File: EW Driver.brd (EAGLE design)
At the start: 103.9 x 81.8 mm, 42 parts, among them Q1 IRF840S, U1 MAX1771ESA, U2 ARDUINOMICRO, U5 HV507, U6 HV507, X1 BNCHOR

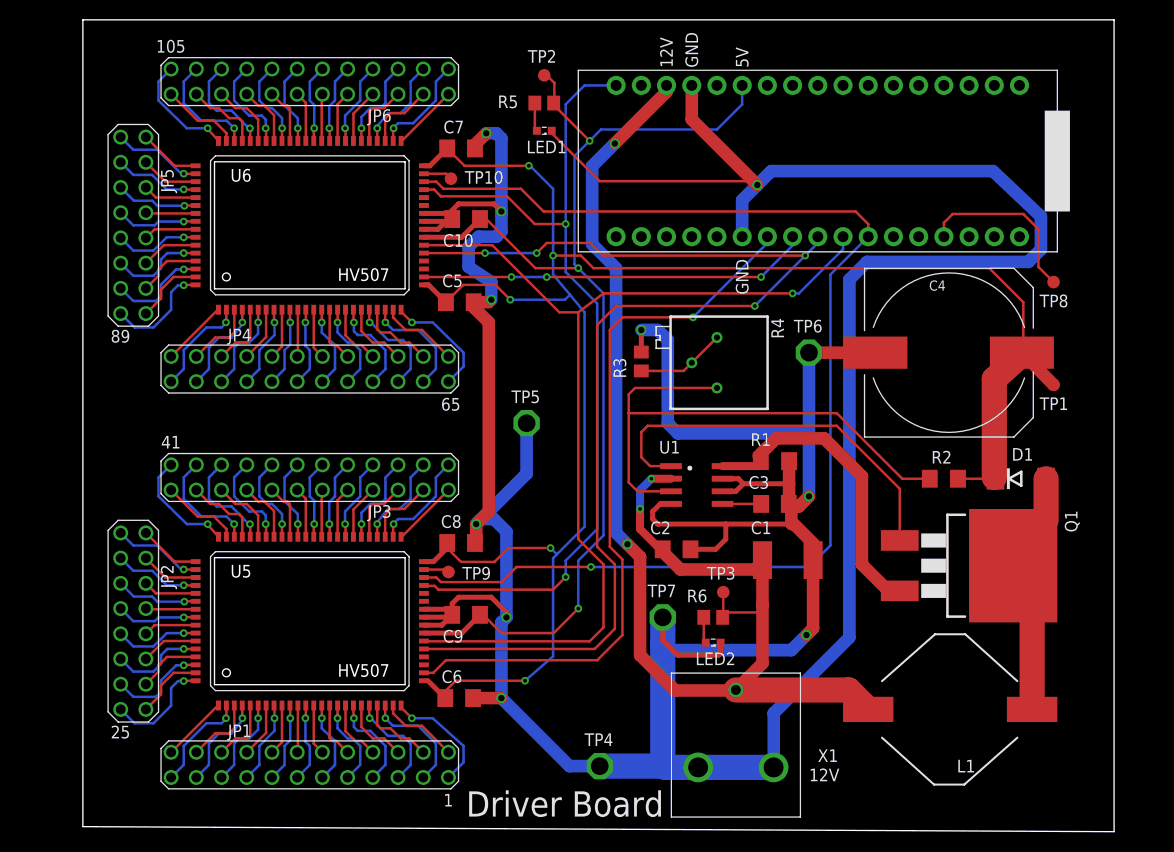
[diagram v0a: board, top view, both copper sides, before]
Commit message: Added standoff mounting holes and increased board size.
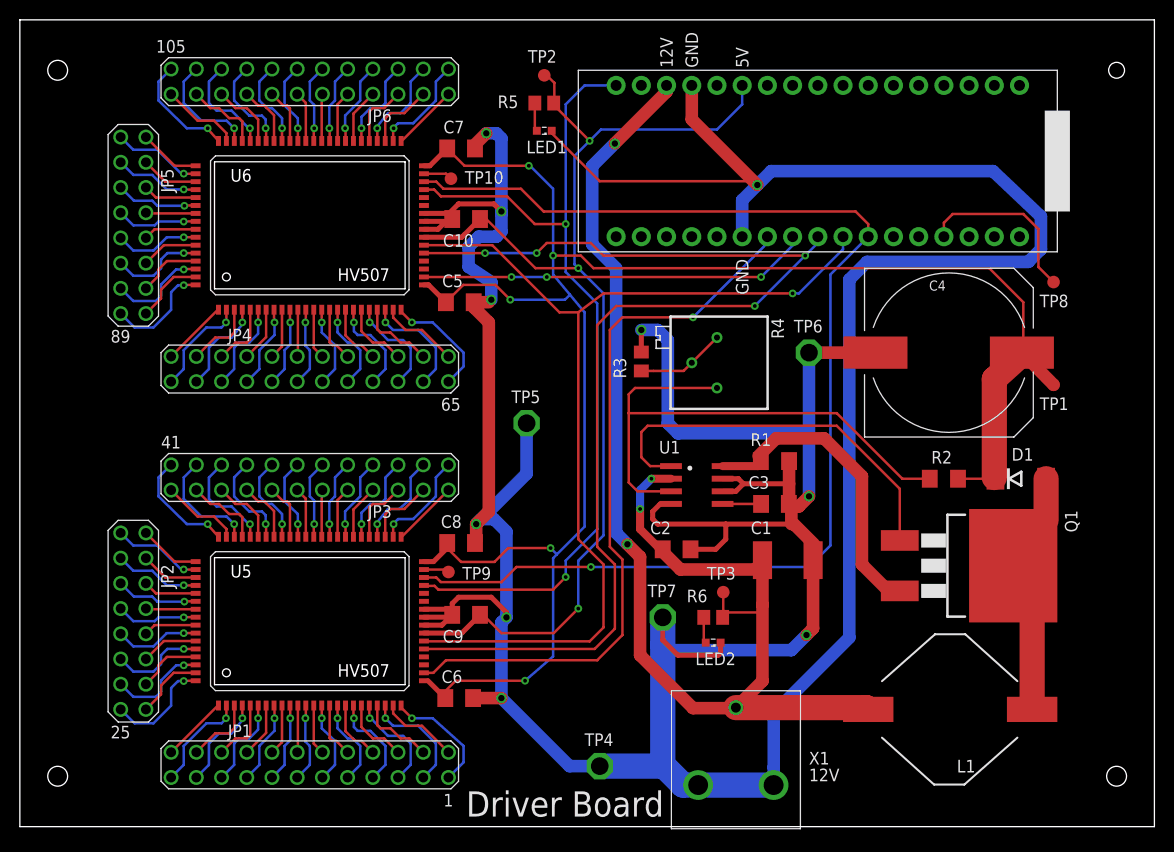
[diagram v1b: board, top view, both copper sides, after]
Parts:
- moved X1 1.78 mm to (65.8, 4.19)
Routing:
- net GND: track 447.1 -> 449.6 mm
- net PP12V0: track 132.0 -> 133.8 mm
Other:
- board size 103.9 x 81.8 mm -> 114.3 x 81.3 mm
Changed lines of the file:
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@@
 <setting verticaltext="up"/>
 </settings>
-<grid distance="0.01" unitdist="inch" unit="inch" style="lines" multiple="1" display="yes" altdistance="0.0025" altunitdist="inch" altunit="inch"/>
+<grid distance="0.5" unitdist="mm" unit="mm" style="lines" multiple="1" display="yes" altdistance="0.0025" altunitdist="inch" altunit="inch"/>
 <layers>
 <layer number="1" name="Top" color="4" fill="1" visible="yes" active="yes"/>
@@
 <layer number="27" name="tValues" color="7" fill="1" visible="yes" active="yes"/>
 <layer number="28" name="bValues" color="7" fill="1" visible="yes" active="yes"/>
-<layer number="29" name="tStop" color="7" fill="3" visible="no" active="yes"/>
+<layer number="29" name="tStop" color="7" fill="3" visible="yes" active="yes"/>
 <layer number="30" name="bStop" color="7" fill="6" visible="no" active="yes"/>
 <layer number="31" name="tCream" color="7" fill="4" visible="no" active="yes"/>
@@
 <board>
 <plain>
-<wire x1="0" y1="0" x2="103.886" y2="-0.508" width="0" layer="20"/>
-<wire x1="103.886" y1="-0.508" x2="103.886" y2="81.28" width="0" layer="20"/>
-<wire x1="103.886" y1="81.28" x2="0" y2="81.28" width="0" layer="20"/>
-<wire x1="0" y1="81.28" x2="0" y2="0" width="0" layer="20"/>
+<wire x1="-6.35" y1="0" x2="107.95" y2="0" width="0" layer="20"/>
+<wire x1="107.95" y1="0" x2="107.95" y2="81.28" width="0" layer="20"/>
+<wire x1="107.95" y1="81.28" x2="-6.35" y2="81.28" width="0" layer="20"/>
+<wire x1="-6.35" y1="81.28" x2="-6.35" y2="0" width="0" layer="20"/>
 <text x="36.322" y="2.032" size="1.27" layer="21">1</text>
 <text x="2.794" y="8.89" size="1.27" layer="21">25</text>
@@
 <text x="61.976" y="76.454" size="1.27" layer="21" rot="R90">GND</text>
 <text x="67.056" y="53.594" size="1.27" layer="21" rot="R90">GND</text>
+<hole x="-2.54" y="5.08" drill="2"/>
+<hole x="-2.54" y="76.2" drill="2"/>
+<hole x="104.14" y="76.2" drill="1.6"/>
+<hole x="104.14" y="5.08" drill="2"/>
 </plain>
 <attributes>
@@
 <element name="U5" library="mimi" package="HV507PG-G" value="HV507" x="22.86" y="20.701"/>
 <element name="U6" library="mimi" package="HV507PG-G" value="HV507" x="22.86" y="60.579"/>
-<element name="X1" library="mimi" package="BNC_HOR" value="BNCHOR" x="65.786" y="5.969" smashed="yes">
-<attribute name="NAME" x="74.033" y="6.516" size="1.27" layer="25"/>
+<element name="X1" library="mimi" package="BNC_HOR" value="BNCHOR" x="65.786" y="4.191" smashed="yes">
+<attribute name="NAME" x="73.144" y="6.262" size="1.27" layer="25"/>
 </element>
 <element name="C7" library="eagle-ltspice" package="C1206" value="0.1u" x="38.1" y="68.326" smashed="yes">
@@
 <contactref element="C9" pad="2"/>
 <contactref element="C10" pad="2"/>
-<wire x1="61.986" y1="5.969" x2="69.586" y2="5.969" width="2.54" layer="16"/>
-<wire x1="61.986" y1="5.969" x2="58.674" y2="5.969" width="2.54" layer="16"/>
+<wire x1="61.986" y1="4.191" x2="69.586" y2="4.191" width="2.54" layer="16"/>
+<wire x1="61.986" y1="4.191" x2="60.452" y2="4.191" width="2.54" layer="16"/>
 <wire x1="58.42" y1="18.288" x2="58.42" y2="6.223" width="2.54" layer="16"/>
-<wire x1="58.42" y1="6.223" x2="58.674" y2="5.969" width="2.54" layer="16"/>
+<wire x1="58.42" y1="6.223" x2="60.452" y2="4.191" width="2.54" layer="16"/>
 <wire x1="71.145" y1="36.83" x2="71.145" y2="34.544" width="1.27" layer="1"/>
 <wire x1="71.145" y1="34.544" x2="71.145" y2="32.534" width="1.27" layer="1"/>
@@
 <wire x1="77.216" y1="19.05" x2="69.596" y2="11.43" width="1.27" layer="16"/>
 <wire x1="69.596" y1="11.43" x2="69.596" y2="5.979" width="1.27" layer="16"/>
-<wire x1="69.596" y1="5.979" x2="69.586" y2="5.969" width="1.27" layer="16"/>
+<wire x1="69.596" y1="5.979" x2="69.586" y2="4.191" width="1.27" layer="16"/>
 <wire x1="61.341" y1="74.676" x2="61.341" y2="71.247" width="1.27" layer="1"/>
 <wire x1="61.341" y1="71.247" x2="67.945" y2="64.643" width="1.27" layer="1"/>
@@
 <contactref element="X1" pad="1"/>
 <contactref element="U2" pad="P$20"/>
-<wire x1="65.786" y1="13.769" x2="77.1618" y2="13.769" width="2.54" layer="1"/>
-<wire x1="77.1618" y1="13.769" x2="79.1198" y2="11.811" width="2.54" layer="1"/>
+<wire x1="65.786" y1="11.991" x2="78.9398" y2="11.991" width="2.54" layer="1"/>
+<wire x1="78.9398" y1="11.991" x2="79.1198" y2="11.811" width="2.54" layer="1"/>
 <wire x1="58.417" y1="27.94" x2="57.912" y2="28.194" width="0.8128" layer="1"/>
 <wire x1="57.912" y1="28.194" x2="56.134" y2="29.972" width="0.8128" layer="1"/>
@@
 <contactref element="TP3" pad="TP"/>
 <wire x1="68.465" y1="26.8495" x2="68.465" y2="22.352" width="1.27" layer="1"/>
-<wire x1="68.465" y1="22.352" x2="68.465" y2="16.448" width="1.27" layer="1"/>
-<wire x1="68.465" y1="16.448" x2="65.786" y2="13.769" width="1.27" layer="1"/>
+<wire x1="68.465" y1="22.352" x2="68.465" y2="14.67" width="1.27" layer="1"/>
+<wire x1="68.465" y1="14.67" x2="65.786" y2="11.991" width="1.27" layer="1"/>
 <wire x1="64.947" y1="21.579" x2="64.45" y2="21.082" width="0.254" layer="1"/>
 <wire x1="64.516" y1="23.622" x2="64.516" y2="21.148" width="0.254" layer="1"/>
@@
 <wire x1="54.864" y1="28.448" x2="56.134" y2="27.178" width="1.27" layer="1"/>
 <wire x1="56.134" y1="27.178" x2="56.134" y2="17.272" width="1.27" layer="1"/>
-<wire x1="56.134" y1="17.272" x2="59.69" y2="13.716" width="1.27" layer="1"/>
-<wire x1="59.69" y1="13.716" x2="65.733" y2="13.716" width="1.27" layer="1"/>
-<wire x1="65.733" y1="13.716" x2="65.786" y2="13.769" width="1.27" layer="1"/>
+<wire x1="56.134" y1="17.272" x2="61.468" y2="11.938" width="1.27" layer="1"/>
+<wire x1="61.468" y1="11.938" x2="65.733" y2="11.938" width="1.27" layer="1"/>
+<wire x1="65.733" y1="11.938" x2="65.786" y2="11.991" width="1.27" layer="1"/>
 </signal>
 <signal name="N$1">
